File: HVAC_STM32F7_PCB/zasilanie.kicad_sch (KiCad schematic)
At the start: 34 parts, among them J1 DC_Jack_5.5x2.1mm, Q1 IRLML9301, SW1 SLW-1276864-4A-D, U1 LM2596S-5, U2 LM2596S-3.3

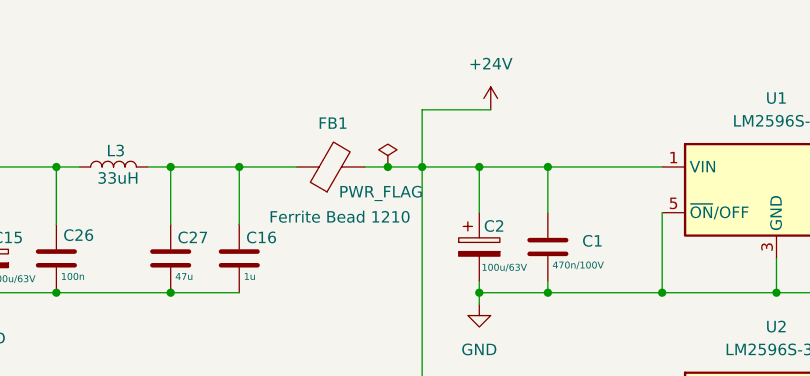
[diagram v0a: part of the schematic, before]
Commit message: ADD Poprawki PCB layout TODO zasilanie toru wyjciowego, podpisy elementow i kosmetyka
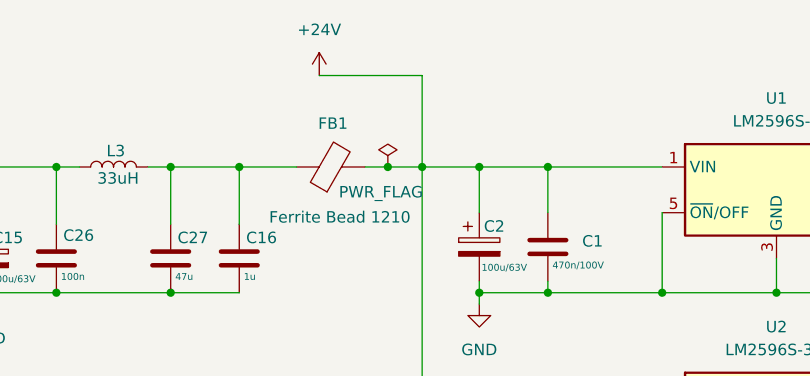
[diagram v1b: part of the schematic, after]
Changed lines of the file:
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@@
 	(wire
 		(pts
-			(xy 165.1 69.85) (xy 165.1 76.2)
+			(xy 165.1 66.04) (xy 165.1 76.2)
 		)
 		(stroke
@@
 	(wire
 		(pts
-			(xy 165.1 69.85) (xy 172.72 69.85)
+			(xy 165.1 66.04) (xy 153.67 66.04)
 		)
 		(stroke
@@
 	(symbol
 		(lib_id "power:+24V")
-		(at 172.72 69.85 0)
+		(at 153.67 66.04 0)
 		(unit 1)
 		(exclude_from_sim no)
@@
 		(fields_autoplaced yes)
 		(property "Reference" "#PWR011"
-			(at 172.72 73.66 0)
+			(at 153.67 69.85 0)
 			(effects
 				(font
@@
 		)
 		(property "Value" "+24V"
-			(at 172.72 64.77 0)
+			(at 153.67 60.96 0)
 			(effects
 				(font
@@
 		)
 		(property "Footprint" ""
-			(at 172.72 69.85 0)
+			(at 153.67 66.04 0)
 			(effects
 				(font
@@
 		)
 		(property "Datasheet" ""
-			(at 172.72 69.85 0)
+			(at 153.67 66.04 0)
 			(effects
 				(font
@@
 		)
 		(property "Description" "Power symbol creates a global label with name \"+24V\""
-			(at 172.72 69.85 0)
+			(at 153.67 66.04 0)
 			(effects
 				(font

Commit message: ADD final pcb version for review, god bless
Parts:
- FB1: value Ferrite Bead 1210 -> Ferrite
- SW1: value SLW-1276864-4A-D -> ON/OFF
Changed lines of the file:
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@@
 			)
 		)
-		(property "Value" "SLW-1276864-4A-D"
+		(property "Value" "ON/OFF"
 			(at 101.6 72.39 0)
 			(effects
@@
 			)
 		)
-		(property "Value" "Ferrite Bead 1210"
+		(property "Value" "Ferrite"
 			(at 155.956 81.788 90)
 			(effects
@@
 			)
 		)
-		(property "Description" "Ferrite bead"
+		(property "Description" "Ferrite Bead 1210"
 			(at 154.94 76.2 0)
 			(effects

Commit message: ADD hopefully finished pcb project
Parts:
- removed R5: 180K, Resistor_SMD:R_0805_2012Metric_Pad1.20x1.40mm_HandSolder, symbol Device:R
- D4: value SOD322 -> 1N4742A; footprint Diode_SMD:D_SOD-323F -> Diode_THT:D_DO-41_SOD81_P2.54mm_Vertical_AnodeUp
- Q1: value IRLML9301 -> AO4407A; footprint Package_TO_SOT_SMD:SOT-23 -> własne:PowerPAK_SO-8_Single
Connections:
- net at D4.1 (K), Q1.2 (S): now also SW1.1 (A); no longer D3.2 (A2), F1.2
- net at Q1.3 (D): now also D3.2 (A2), F1.2; no longer SW1.1 (A)
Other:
- moved on the sheet: D4, Q1, R4
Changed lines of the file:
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@@
 	)
 	(junction
-		(at 171.45 76.2)
+		(at 93.98 76.2)
 		(diameter 0)
 		(color 0 0 0 0)
 	)
 	(junction
-		(at 179.07 90.17)
+		(at 171.45 76.2)
 		(diameter 0)
 		(color 0 0 0 0)
 	)
 	(junction
-		(at 137.16 76.2)
+		(at 179.07 90.17)
 		(diameter 0)
 		(color 0 0 0 0)
 	)
 	(junction
-		(at 78.74 90.17)
+		(at 137.16 76.2)
 		(diameter 0)
 		(color 0 0 0 0)
@@
 	)
 	(junction
-		(at 78.74 76.2)
-		(diameter 0)
-		(color 0 0 0 0)
-	)
-	(junction
 		(at 240.03 106.68)
 		(diameter 0)
@@
 	)
 	(junction
-		(at 73.66 76.2)
-		(diameter 0)
-		(color 0 0 0 0)
-	)
-	(junction
 		(at 191.77 90.17)
 		(diameter 0)
@@
 	)
 	(junction
-		(at 88.9 90.17)
+		(at 82.55 90.17)
 		(diameter 0)
 		(color 0 0 0 0)
@@
 	(wire
 		(pts
-			(xy 78.74 76.2) (xy 83.82 76.2)
-		)
-		(stroke
-			(width 0)
-			(type default)
-		)
-	)
-	(wire
-		(pts
 			(xy 179.07 88.9) (xy 179.07 90.17)
 		)
@@
 	(wire
 		(pts
-			(xy 73.66 76.2) (xy 78.74 76.2)
-		)
-		(stroke
-			(width 0)
-			(type default)
-		)
-	)
-	(wire
-		(pts
 			(xy 191.77 81.28) (xy 191.77 90.17)
 		)
@@
 	(wire
 		(pts
-			(xy 62.23 99.06) (xy 88.9 99.06)
+			(xy 62.23 99.06) (xy 82.55 99.06)
 		)
 		(stroke
@@
 	(wire
 		(pts
-			(xy 73.66 90.17) (xy 73.66 83.82)
+			(xy 93.98 90.17) (xy 93.98 87.63)
 		)
 		(stroke
@@
 	(wire
 		(pts
+			(xy 93.98 76.2) (xy 93.98 80.01)
+		)
+		(stroke
+			(width 0)
+			(type default)
+		)
+	)
+	(wire
+		(pts
 			(xy 165.1 66.04) (xy 153.67 66.04)
 		)
@@
 	(wire
 		(pts
-			(xy 73.66 90.17) (xy 78.74 90.17)
+			(xy 93.98 90.17) (xy 82.55 90.17)
 		)
 		(stroke
@@
 	(wire
 		(pts
-			(xy 62.23 76.2) (xy 73.66 76.2)
+			(xy 62.23 76.2) (xy 77.47 76.2)
 		)
 		(stroke
@@
 	(wire
 		(pts
-			(xy 78.74 90.17) (xy 88.9 90.17)
+			(xy 137.16 76.2) (xy 137.16 82.55)
 		)
 		(stroke
@@
 	(wire
 		(pts
-			(xy 137.16 76.2) (xy 137.16 82.55)
+			(xy 165.1 101.6) (xy 171.45 101.6)
 		)
 		(stroke
@@
 	(wire
 		(pts
-			(xy 165.1 101.6) (xy 171.45 101.6)
+			(xy 45.72 81.28) (xy 45.72 99.06)
 		)
 		(stroke
@@
 	(wire
 		(pts
-			(xy 45.72 81.28) (xy 45.72 99.06)
+			(xy 93.98 76.2) (xy 87.63 76.2)
 		)
 		(stroke
@@
 	(wire
 		(pts
-			(xy 88.9 90.17) (xy 88.9 83.82)
+			(xy 82.55 83.82) (xy 82.55 90.17)
 		)
 		(stroke
@@
 	(wire
 		(pts
-			(xy 78.74 83.82) (xy 78.74 90.17)
-		)
-		(stroke
-			(width 0)
-			(type default)
-		)
-	)
-	(wire
-		(pts
 			(xy 240.03 90.17) (xy 248.92 90.17)
 		)
@@
 	(wire
 		(pts
-			(xy 88.9 99.06) (xy 88.9 97.79)
+			(xy 82.55 99.06) (xy 82.55 97.79)
 		)
 		(stroke
@@
 	(symbol
 		(lib_id "Transistor_FET:IRLML6402")
-		(at 88.9 78.74 270)
-		(mirror x)
+		(at 82.55 78.74 90)
 		(unit 1)
 		(exclude_from_sim no)
@@
 		(dnp no)
 		(property "Reference" "Q1"
-			(at 88.9 72.39 90)
+			(at 82.55 72.39 90)
 			(effects
 				(font
@@
 			)
 		)
-		(property "Value" "IRLML9301"
-			(at 88.9 69.85 90)
+		(property "Value" "AO4407A"
+			(at 82.55 69.85 90)
 			(effects
 				(font
@@
 			)
 		)
-		(property "Footprint" "Package_TO_SOT_SMD:SOT-23"
-			(at 86.995 73.66 0)
+		(property "Footprint" "własne:PowerPAK_SO-8_Single"
+			(at 84.455 73.66 0)
 			(effects
 				(font
@@
 			)
 		)
-		(property "Datasheet" "https://www.infineon.com/dgdl/irlml6402pbf.pdf?fileId=5546d462533600a401535668d5c2263c"
-			(at 85.09 73.66 0)
+		(property "Datasheet" "~"
+			(at 86.36 73.66 0)
 			(effects
 				(font
@@
 			)
 		)
-		(property "Description" "-3.7A Id, -20V Vds, 65mOhm Rds, P-Channel HEXFET Power MOSFET, SOT-23"
-			(at 88.9 78.74 0)
+		(property "Description" "~"
+			(at 82.55 78.74 0)
 			(effects
 				(font
@@
 	(symbol
 		(lib_id "Device:R")
-		(at 88.9 93.98 0)
+		(at 82.55 93.98 0)
 		(unit 1)
 		(exclude_from_sim no)
@@
 		(fields_autoplaced yes)
 		(property "Reference" "R4"
-			(at 91.44 92.7099 0)
+			(at 85.09 92.7099 0)
 			(effects
 				(font
@@
 		)
 		(property "Value" "75K"
-			(at 91.44 95.2499 0)
+			(at 85.09 95.2499 0)
 			(effects
 				(font
@@
 		)
 		(property "Footprint" "Resistor_SMD:R_0805_2012Metric_Pad1.20x1.40mm_HandSolder"
-			(at 87.122 93.98 90)
+			(at 80.772 93.98 90)
 			(effects
 				(font
@@
 		)
 		(property "Datasheet" "~"
-			(at 88.9 93.98 0)
+			(at 82.55 93.98 0)
 			(effects
 				(font
@@
 		)
 		(property "Description" "Resistor"
-			(at 88.9 93.98 0)
+			(at 82.55 93.98 0)
 			(effects
 				(font
@@
 	)
 	(symbol
-		(lib_id "Device:R")
-		(at 78.74 80.01 0)
-		(unit 1)
-		(exclude_from_sim no)
-		(in_bom yes)
-		(on_board yes)
-		(dnp no)
-		(fields_autoplaced yes)
-		(property "Reference" "R5"
-			(at 81.28 78.7399 0)
-			(effects
-				(font
-					(size 1.27 1.27)
-				)
-				(justify left)
-			)
-		)
-		(property "Value" "180K"
-			(at 81.28 81.2799 0)
-			(effects
-				(font
-					(size 1.27 1.27)
-				)
-				(justify left)
-			)
-		)
-		(property "Footprint" "Resistor_SMD:R_0805_2012Metric_Pad1.20x1.40mm_HandSolder"
-			(at 76.962 80.01 90)
-			(effects
-				(font
-					(size 1.27 1.27)
-				)
-				(hide yes)
-			)
-		)
-		(property "Datasheet" "~"
-			(at 78.74 80.01 0)
-			(effects
-				(font
-					(size 1.27 1.27)
-				)
-				(hide yes)
-			)
-		)
-		(property "Description" "Resistor"
-			(at 78.74 80.01 0)
-			(effects
-				(font
-					(size 1.27 1.27)
-				)
-				(hide yes)
-			)
-		)
-		(pin "2"
-		)
-		(pin "1"
-		)
-		(instances
-			(project "HVAC_STM32F7_PCB"
-				(path "/79f65717-d4aa-4d9b-9389-67dd3cbc0c4f/b2dfabe3-5da3-487e-82ba-41cecc037238"
-					(reference "R5")
-					(unit 1)
-				)
-			)
-		)
-	)
-	(symbol
 		(lib_id "power:+24V")
 		(at 153.67 66.04 0)
@@
 	(symbol
 		(lib_id "Device:D_Zener")
-		(at 73.66 80.01 270)
+		(at 93.98 83.82 270)
 		(unit 1)
 		(exclude_from_sim no)
@@
 		(dnp no)
 		(property "Reference" "D4"
-			(at 69.342 80.264 90)
+			(at 89.662 84.074 90)
 			(effects
 				(font
@@
 			)
 		)
-		(property "Value" "SOD322"
-			(at 66.04 82.55 90)
+		(property "Value" "1N4742A"
+			(at 86.36 86.36 90)
 			(effects
 				(font
@@
 			)
 		)
-		(property "Footprint" "Diode_SMD:D_SOD-323F"
-			(at 73.66 80.01 0)
+		(property "Footprint" "Diode_THT:D_DO-41_SOD81_P2.54mm_Vertical_AnodeUp"
+			(at 93.98 83.82 0)
 			(effects
 				(font
@@
 		)
 		(property "Datasheet" "~"
-			(at 73.66 80.01 0)
+			(at 93.98 83.82 0)
 			(effects
 				(font
@@
 		)
 		(property "Description" "Zener diode"
-			(at 73.66 80.01 0)
+			(at 93.98 83.82 0)
 			(effects
 				(font

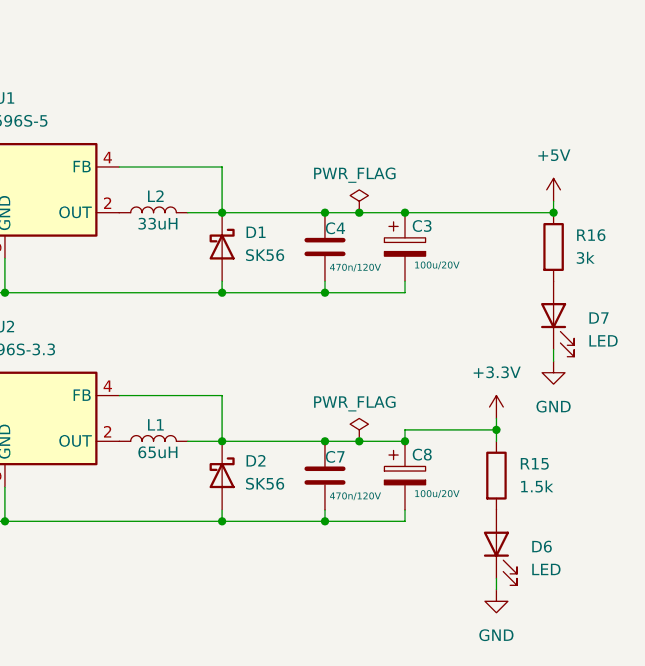
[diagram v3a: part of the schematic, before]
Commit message: ADD: poprawki pcb, nowe gerbery
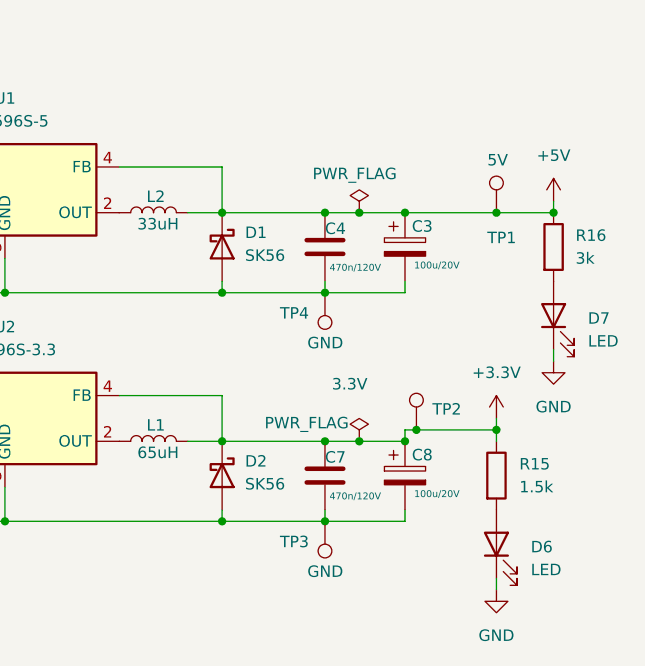
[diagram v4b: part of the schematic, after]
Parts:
- added TP1: 5V, TestPoint:TestPoint_Loop_D1.80mm_Drill1.0mm_Beaded, symbol Connector:TestPoint
- added TP2: 3.3V, TestPoint:TestPoint_Loop_D1.80mm_Drill1.0mm_Beaded, symbol Connector:TestPoint
- added TP3, TP4: GND, TestPoint:TestPoint_Loop_D1.80mm_Drill1.0mm_Beaded, symbol Connector:TestPoint
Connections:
- net +3.3V: now also TP2.1
- net +5V: now also TP1.1
- net GND: now also TP3.1, TP4.1
